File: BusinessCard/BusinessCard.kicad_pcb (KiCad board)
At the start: 2 copper layers, 4 parts, among them U1 ATtiny3217-M

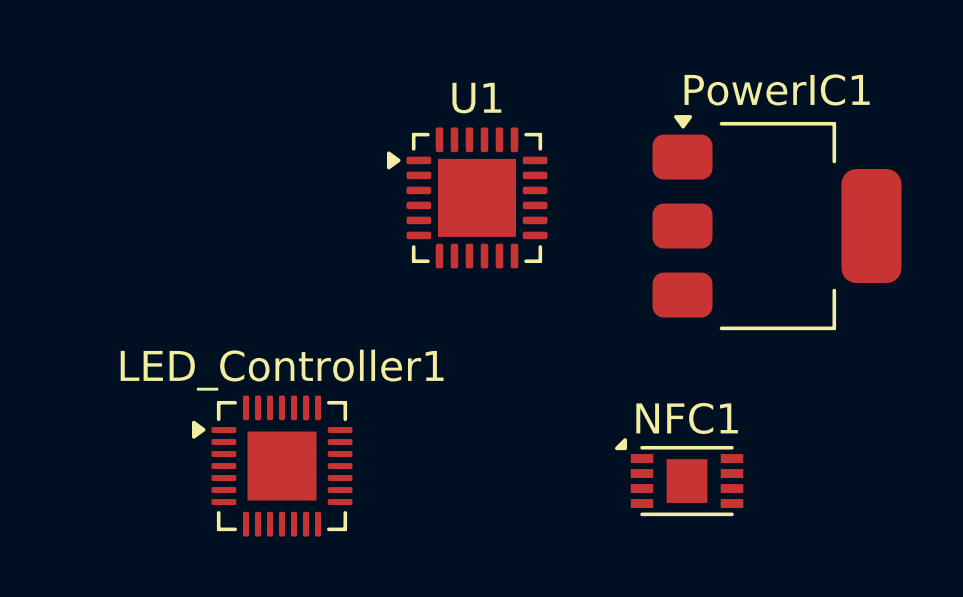
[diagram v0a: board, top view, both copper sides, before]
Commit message: NFC only design
removed unnecessary items, switched out NFC capacitor, added footprints, Antenna loop footprint WIP
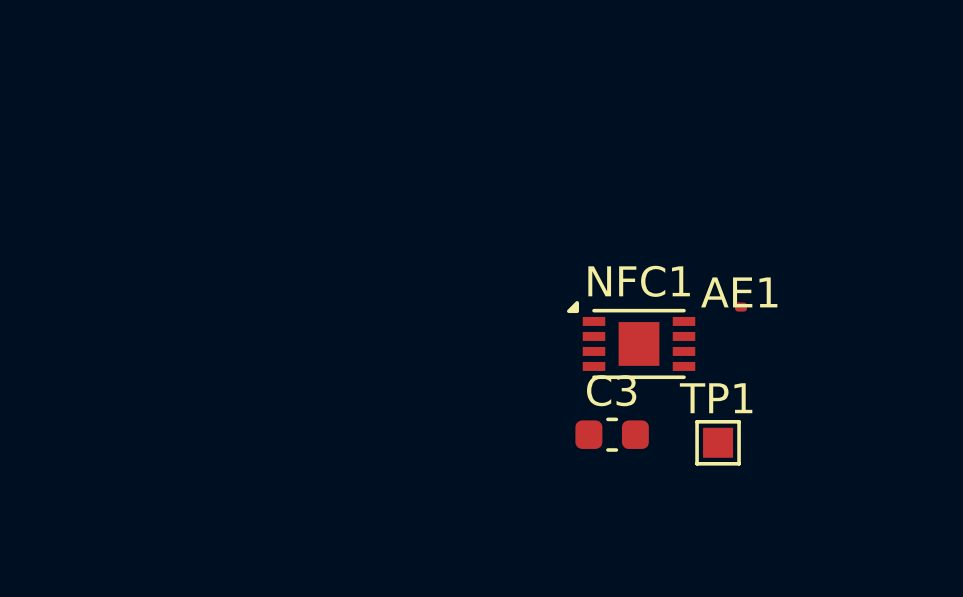
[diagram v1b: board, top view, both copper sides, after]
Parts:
- removed LED_Controller1: IS31FL3731-QF, Package_DFN_QFN:QFN-28-1EP_4x4mm_P0.4mm_EP2.3x2.3mm
- removed PowerIC1: AMS1117-3.3, Package_TO_SOT_SMD:SOT-223-3_TabPin2
- removed U1: ATtiny3217-M, Package_DFN_QFN:QFN-24-1EP_4x4mm_P0.5mm_EP2.6x2.6mm
- added AE1: Antenna_Loop, Library:antenna_pad, F.Cu at (146.8, 89.8)
- added C3: 1uF, Capacitor_SMD:C_0603_1608Metric, F.Cu at (142.5, 94.0)
- added TP1: TestPoint, TestPoint:TestPoint_Pad_1.0x1.0mm, F.Cu at (146.0, 94.2)
- NFC1: value ST25DV04K-IER8C3 -> ST25DV04K-IER6C3
- moved NFC1 4.84 mm to (143.4, 90.9)
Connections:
- NFC1 pad 5: /SDA -> unconnected-(NFC1-SDA-Pad5)
- NFC1 pad 6: /SCL -> unconnected-(NFC1-SCL-Pad6)
- NFC1 pad 7: /GPO -> unconnected-(NFC1-GPO-Pad7)
- NFC1 pad 8: +3.3V -> unconnected-(NFC1-VCC-Pad8)
